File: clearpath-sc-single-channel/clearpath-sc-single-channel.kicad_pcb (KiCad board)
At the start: 2 copper layers, 74.8 x 49.8 mm, 58 parts, among them P1 MOLEX_MICROFIT_JR_RH_2x1_WAY, P2 MOLEX_MICROFIT_JR_RH_2x2_WAY, P3 MOLEX_MICROFIT_JR_RH_2x2_WAY, P4 MOLEX_MICROFIT_JR_RH_2x4_WAY, P5 CONN_01X08, Q1 MMBT5401, Q2 MMBTA06, U1 LM317LCPK, U2 FT230XS-R, U3 USBLC6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

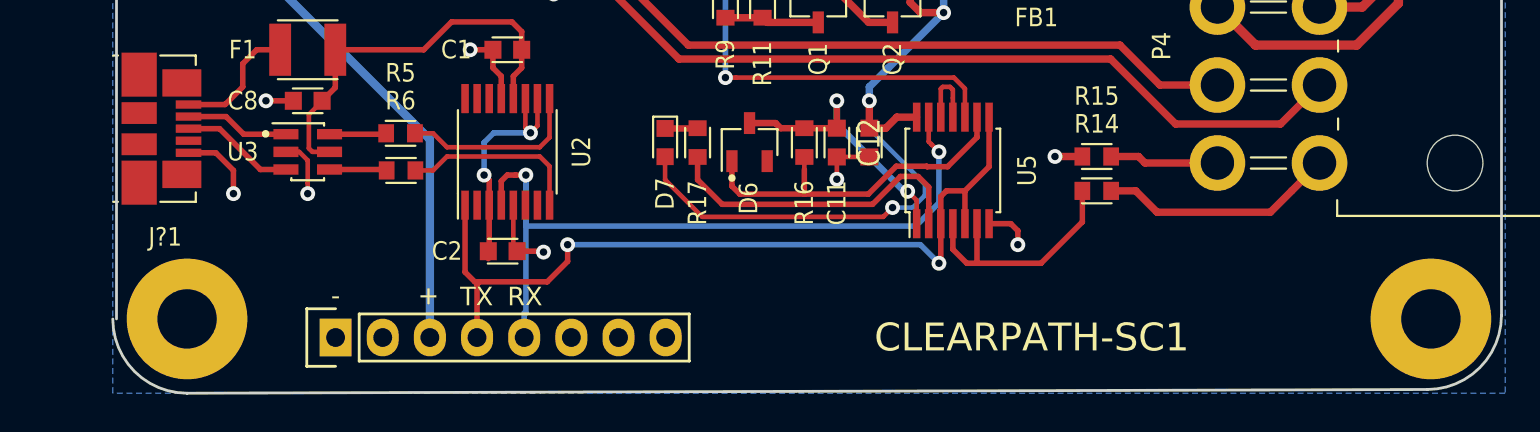
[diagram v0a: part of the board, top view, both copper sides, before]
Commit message: Fixed gap in outline layer, exported gerbers
Fixes issue where copper layers don't export properly.
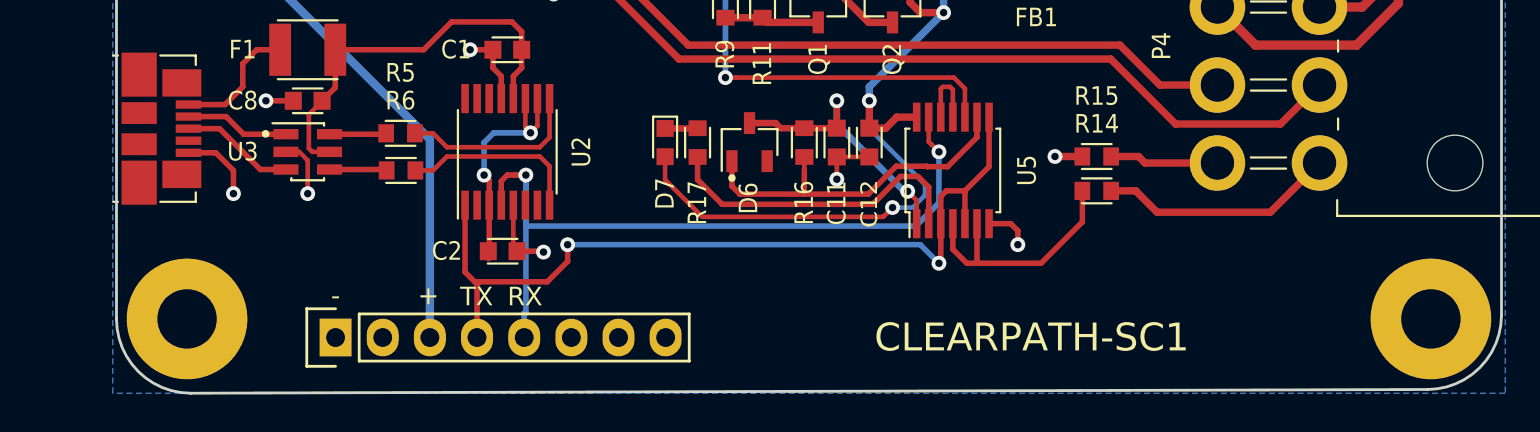
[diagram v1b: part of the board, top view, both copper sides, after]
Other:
- board size 74.8 x 49.8 mm -> 74.6 x 49.8 mm
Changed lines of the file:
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@@
     (46 B.CrtYd user)
     (47 F.CrtYd user)
-    (48 B.Fab user)
+    (48 B.Fab user hide)
     (49 F.Fab user hide)
   )
@@
     (aux_axis_origin 100 100)
     (grid_origin 100 100)
-    (visible_elements 7FFEFFFF)
+    (visible_elements 7FFDFFFF)
     (pcbplotparams
       (layerselection 0x313fc_ffffffff)
@@
       (drillshape 0)
       (scaleselection 1)
-      (outputdirectory /home/scott/projects/clearpath-sc-single/gerbers/))
+      (outputdirectory ../gerbers/))
   )
   (net 0 "")
@@
     (clearance 0.2)
     (attr smd)
-    (fp_text reference J?1 (at 0.07 5.84 180) (layer F.SilkS)
+    (fp_text reference J?1 (at 0.07 5.84) (layer F.SilkS) hide
       (effects (font (size 1 0.9) (thickness 0.13)))
     )
@@
     (autoplace_cost180 10)
     (attr smd)
-    (fp_text reference C12 (at 0 0 270) (layer F.SilkS)
-      (effects (font (size 1.2 0.96) (thickness 0.12)))
+    (fp_text reference C12 (at 3.3 0 270) (layer F.SilkS)
+      (effects (font (size 0.9 0.96) (thickness 0.13)))
     )
     (fp_text value 100NF_X7R_1608M (at 0 0 270) (layer F.SilkS) hide
@@
   (gr_arc (start 170.8 104.2) (end 174.8 104.2) (angle -90) (layer Edge.Cuts) (width 0.15))
   (gr_arc (start 170.8 145.8) (end 170.8 149.8) (angle -90) (layer Edge.Cuts) (width 0.15))
-  (gr_arc (start 104 146) (end 100 146) (angle -90) (layer Edge.Cuts) (width 0.15))
+  (gr_arc (start 104.2 146) (end 100.2 146) (angle -90) (layer Edge.Cuts) (width 0.15))
   (gr_arc (start 104.2 104.2) (end 100.2 104.2) (angle 90) (layer Edge.Cuts) (width 0.15))
   (gr_line (start 174.8 145.8) (end 174.8 104.2) (layer Edge.Cuts) (width 0.15))
-  (gr_line (start 104 150) (end 170.8 149.8) (layer Edge.Cuts) (width 0.15))
+  (gr_line (start 104.2 150) (end 170.8 149.8) (layer Edge.Cuts) (width 0.15))
   (gr_line (start 100.2 104.2) (end 100.2 146) (layer Edge.Cuts) (width 0.15))
   (gr_line (start 104.2 100.2) (end 170.8 100.2) (layer Edge.Cuts) (width 0.15))
